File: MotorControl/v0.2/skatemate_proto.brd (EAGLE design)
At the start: 72.1 x 81.7 mm, 97 parts, among them IC1 REG1117, U1 DRV8301DCAR, U2 STM32F303XD/XELQFP64, X1 ABM3B

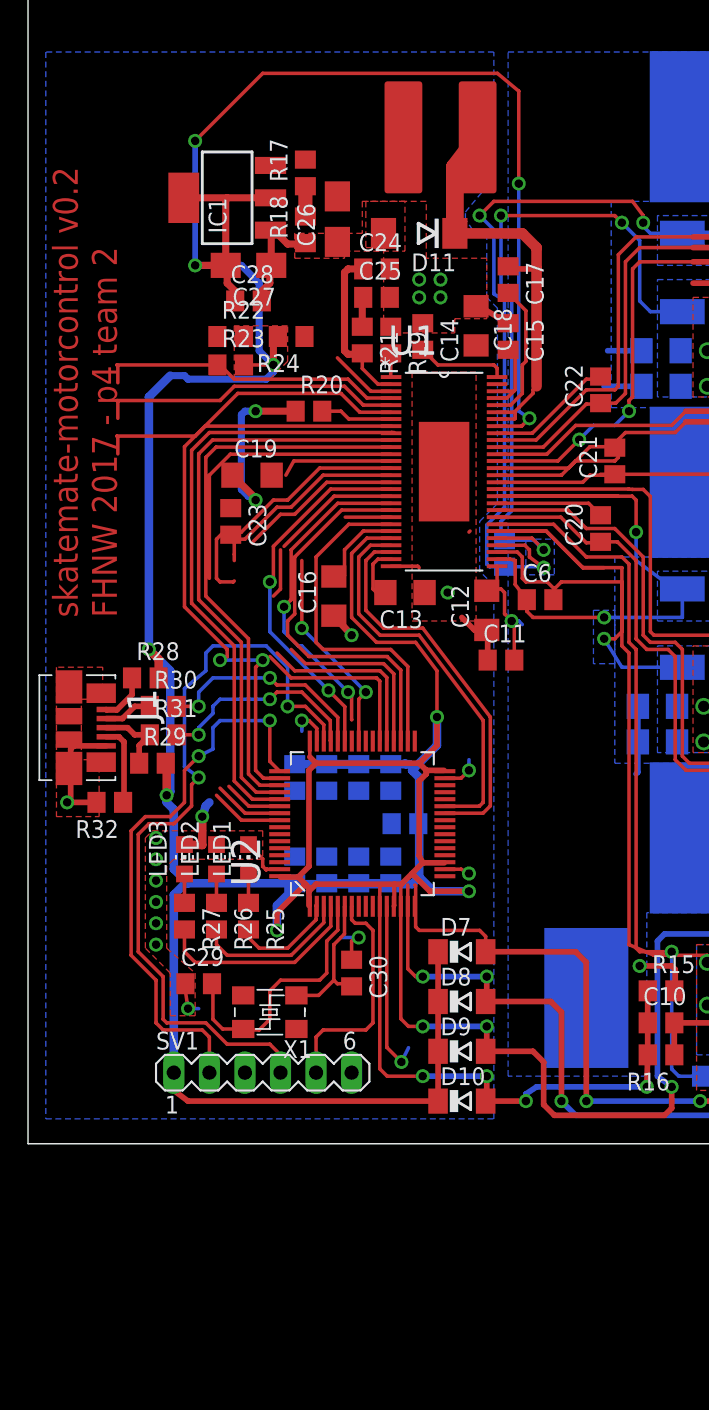
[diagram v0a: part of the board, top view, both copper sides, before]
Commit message: Add RFM module
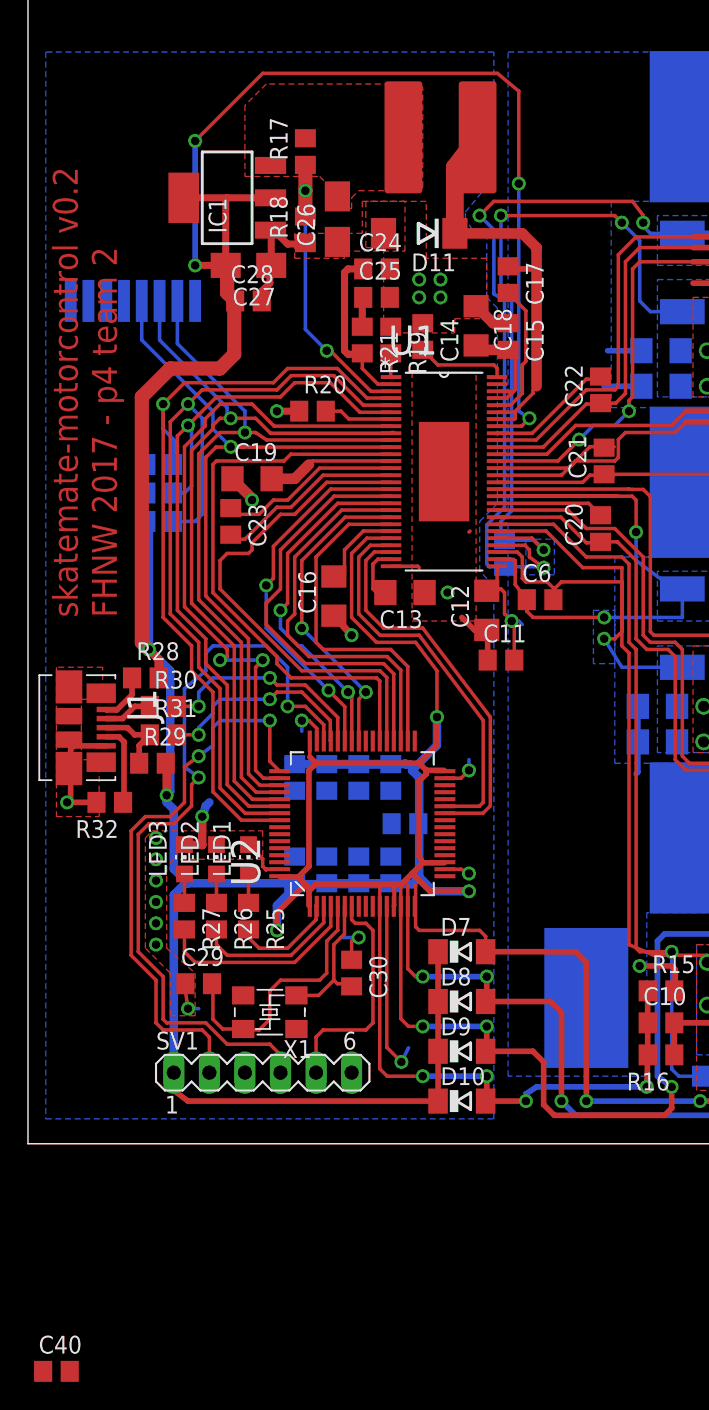
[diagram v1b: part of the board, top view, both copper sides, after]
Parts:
- added C40: 100n, skatemate:C0805
- added U3: RFM75, skatemate:RFM75
- moved R24 13.1 mm to (48.0, 47.2), flipped to the bottom, turned to 0 degrees
- moved R23 12.3 mm to (48.0, 43.2), flipped to the bottom
- moved R22 12.3 mm to (48.0, 45.2), flipped to the bottom
- moved R17 1.52 mm to (58.4, 69.6)
- moved C21 0.76 mm to (79.8, 47.5)
- moved C19 0.25 mm to (54.6, 46.2)
- moved R20 0.25 mm to (58.9, 51.1)
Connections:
- new net RFM_CE: U2.8, U3.3
- new net RFM_IRQ: U2.10, U3.8
- new net RFM_NCS: U2.9, U3.4
- net DRV_SCK: now also U3.5
- net DRV_SDI: now also U3.6
- net DRV_SDO: now also U3.7
- net GND: now also C40.2, U3.1
- net VCC: now also C40.1, U3.2
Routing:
- net DRV_NOCTW: track 26.9 -> 61.3 mm, vias 0 -> 1
- net DRV_PWRGD: track 27.1 -> 57.6 mm, vias 0 -> 1
- net DRV_NFAULT: track 26.9 -> 54.4 mm, vias 0 -> 1
- net GND: track 228.1 -> 210.2 mm
- net DRV_SCK: track 40.0 -> 55.0 mm, vias 0 -> 1
- net N$4: track 6.99 -> 21.5 mm, vias 0 -> 2
- net DRV_SDO: track 41.7 -> 53.5 mm, vias 0 -> 1
- net DRV_SDI: track 43.7 -> 55.2 mm, vias 0 -> 1
- net DRV_EN_GATE: track 24.8 -> 35.9 mm
- net DRV_DCCAL: track 33.8 -> 41.3 mm
- net N$2: track 18.8 -> 13.0 mm
- net INL_A: track 25.5 -> 30.6 mm
- net INH_C: track 18.3 -> 22.7 mm
- net SUPPLY: track 30.6 -> 33.1 mm
- net INH_B: track 23.0 -> 25.1 mm
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- added copper zone on layer 1, net +5V
- removed copper zone on layer 1, net VCC

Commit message: finished all wires and first review
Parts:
- moved C40 92.9 mm to (3.30, 67.6), flipped to the bottom
- moved R15 41.7 mm to (42.2, 11.7), turned to 90 degrees
- moved C30 40.5 mm to (21.3, 13.7), turned to 90 degrees
- moved R20 39.3 mm to (20.1, 56.9)
- moved C16 39.0 mm to (21.8, 43.7)
- moved C1 39.0 mm to (34.0, 46.5)
- moved C11 39.0 mm to (33.8, 38.9)
- moved C14 39.0 mm to (28.2, 62.0)
- moved C17 39.0 mm to (34.3, 66.0)
- moved C19 39.0 mm to (16.0, 51.8)
- moved C24 39.0 mm to (24.9, 66.8)
- moved C25 39.0 mm to (24.9, 64.8)
- moved C26 39.0 mm to (22.1, 70.4)
- moved C27 39.0 mm to (15.7, 67.1)
- moved C28 39.0 mm to (15.7, 64.5)
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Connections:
- net RFM_CE: now also U2.10; no longer U2.8
- net RFM_IRQ: now also U2.8; no longer U2.10
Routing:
- net RFM_IRQ: track 0.00 -> 94.9 mm, vias 0 -> 3
- net RFM_CE: track 0.00 -> 92.9 mm, vias 0 -> 1
- net RFM_NCS: track 0.00 -> 91.5 mm, vias 0 -> 1
- net VCC: track 320.3 -> 277.6 mm, vias 9 -> 12
- net GND: track 210.2 -> 192.2 mm, vias 42 -> 45
- net DRV_NFAULT: track 54.4 -> 61.8 mm
- net DRV_PWRGD: track 57.6 -> 64.8 mm
- net DRV_NOCTW: track 61.3 -> 68.1 mm
- net SN_B: track 45.6 -> 39.3 mm
- net GL_C: track 51.6 -> 57.3 mm
- net BST_BK: track 31.2 -> 34.7 mm
- net SSENSE: track 41.8 -> 38.5 mm
- net N$16: track 9.96 -> 13.1 mm
- net SUPPLY: track 33.1 -> 30.9 mm, vias 2 -> 5
- net BSENSE: track 139.3 -> 137.5 mm
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- added copper zone on layer 1, net N$39
- added copper zone on layer 1, net SUPPLY
- added copper zone on layer 1, net VCC
- added copper zone on layer 16, net VCC
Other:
- board size 72.1 x 81.7 mm -> 72.1 x 91.1 mm

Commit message: pretty 45
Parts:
- moved J1 1.27 mm to (4.32, 34.0)
- moved R32 1.27 mm to (4.57, 28.7)
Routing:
- net VCC: track 277.6 -> 263.6 mm
- net BST_BK: track 34.7 -> 31.7 mm
- net N$22: track 5.75 -> 8.24 mm
- net DRV_SCK: track 55.0 -> 53.0 mm
- net SUPPLY: track 30.9 -> 28.9 mm
- net PH_B: track 34.4 -> 33.1 mm
- net N$25: track 3.63 -> 4.90 mm
- net N$24: track 3.48 -> 4.75 mm
- net N$23: track 5.67 -> 6.94 mm
- net N$10: track 2.93 -> 3.48 mm
- net DRV_NCS: track 46.9 -> 46.3 mm
- net GND: track 192.2 -> 191.9 mm, vias 45 -> 46
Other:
- board text added: "Ω"

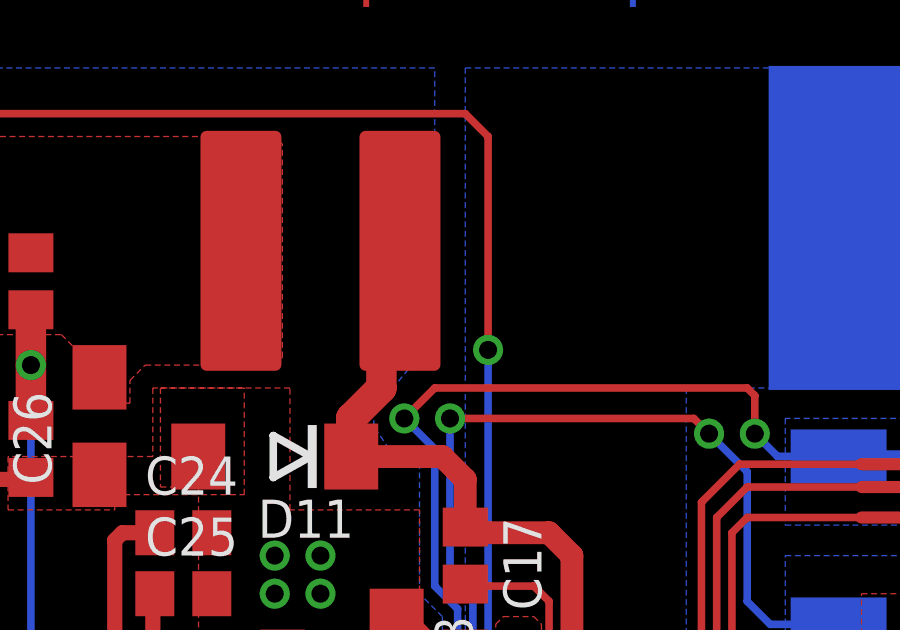
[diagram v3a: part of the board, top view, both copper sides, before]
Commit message: Layout angepasst
C ergänzt
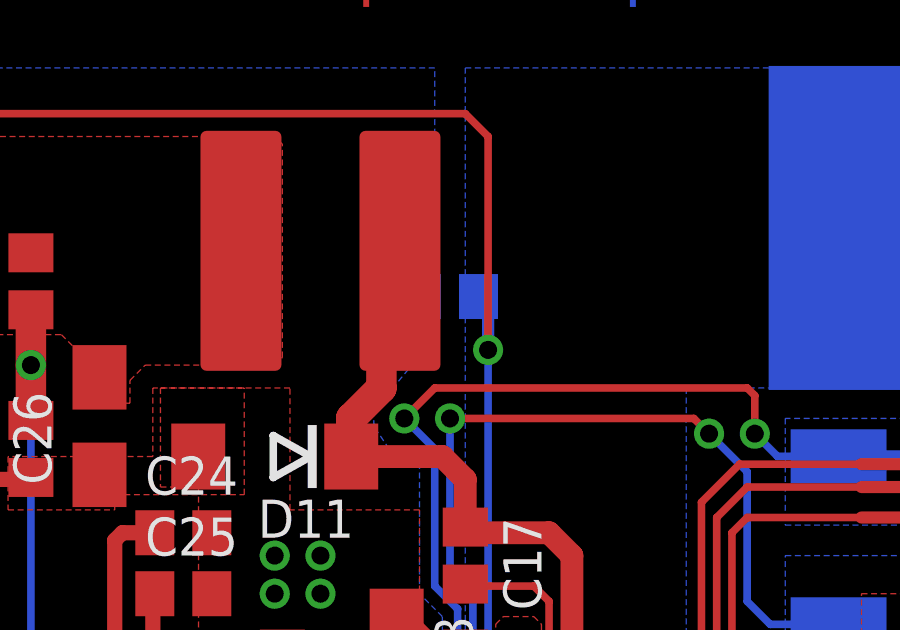
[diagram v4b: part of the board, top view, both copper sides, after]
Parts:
- added C41: 100n, skatemate:C0805
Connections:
- net GND: now also C41.2
- net VCC: now also C41.1
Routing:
- net VCC: track 263.6 -> 265.7 mm
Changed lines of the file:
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@@
 <element name="U3" library="skatemate" package="RFM75" value="RFM75" x="3.048" y="64.516" rot="MR270"/>
 <element name="C40" library="skatemate" package="C0805" value="100n" x="3.302" y="67.564" rot="MR0"/>
+<element name="C41" library="skatemate" package="C0805" value="100n" x="33.782" y="74.676" rot="MR0"/>
 </elements>
 <signals>
@@
 <wire x1="30.936" y1="30.428" x2="31.242" y2="30.734" width="0.254" layer="1"/>
 <wire x1="31.242" y1="30.734" x2="31.242" y2="31.242" width="0.254" layer="1"/>
+<contactref element="C41" pad="2"/>
 </signal>
 <signal name="N$7">
@@
 <wire x1="28.702" y1="34.29" x2="28.702" y2="33.274" width="0.254" layer="1"/>
 <wire x1="28.702" y1="33.274" x2="28.956" y2="33.02" width="0.254" layer="1"/>
+<contactref element="C41" pad="1"/>
+<wire x1="34.732" y1="74.676" x2="35.052" y2="74.676" width="0.4064" layer="16"/>
+<wire x1="35.052" y1="74.676" x2="35.052" y2="72.898" width="0.4064" layer="16"/>
 </signal>
 <signal name="INH_A">

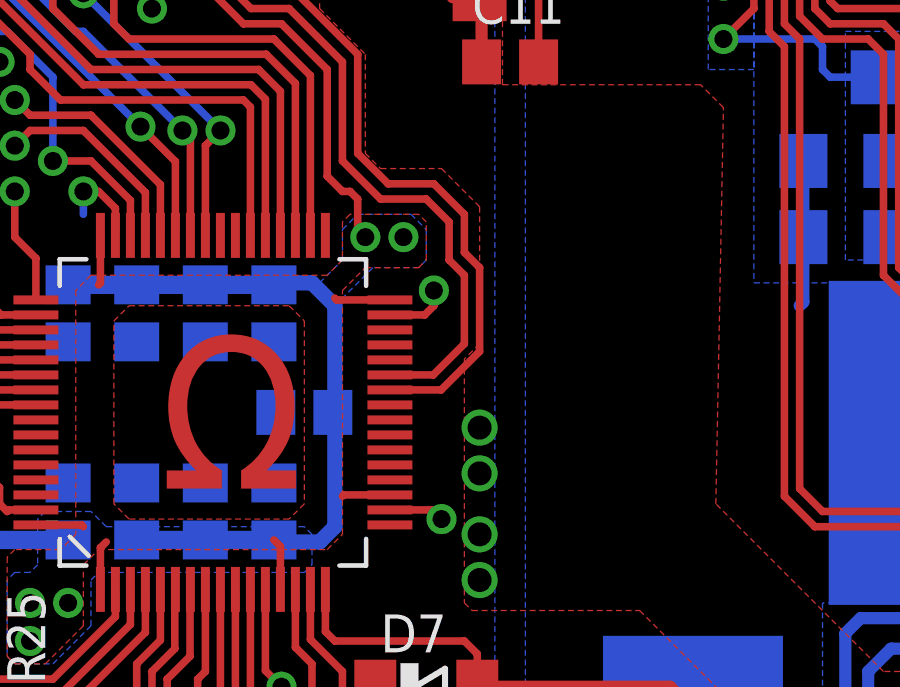
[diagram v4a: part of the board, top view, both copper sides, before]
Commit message: USART3 populated
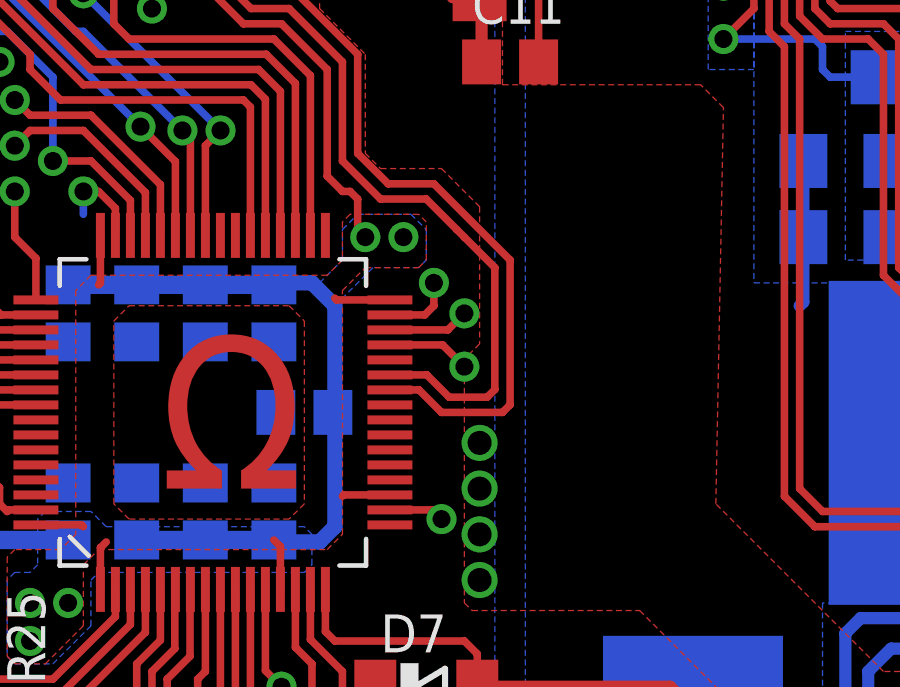
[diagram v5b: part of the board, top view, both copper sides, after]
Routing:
- net DRV_SOB: track 27.6 -> 30.7 mm
- net DRV_SOA: track 27.5 -> 30.5 mm
- net USART3_TX: track 0.00 -> 2.78 mm, vias 0 -> 1
- net USART3_RX: track 0.00 -> 2.71 mm, vias 0 -> 1
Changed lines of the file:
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@@
 <via x="26.162" y="18.034" extent="1-16" drill="0.6"/>
 <wire x1="29.776" y1="30.428" x2="30.936" y2="30.428" width="0.254" layer="1"/>
-<via x="31.242" y="31.242" extent="1-16" drill="0.6"/>
+<via x="31.242" y="31.496" extent="1-16" drill="0.6"/>
 <wire x1="29.776" y1="23.928" x2="31.19" y2="23.928" width="0.254" layer="1"/>
 <via x="31.496" y="23.622" extent="1-16" drill="0.6"/>
@@
 </polygon>
 <via x="32.766" y="21.59" extent="1-16" drill="0.8"/>
-<via x="32.766" y="26.67" extent="1-16" drill="0.8"/>
-<via x="32.766" y="25.146" extent="1-16" drill="0.8"/>
+<via x="32.766" y="26.162" extent="1-16" drill="0.8"/>
+<via x="32.766" y="24.638" extent="1-16" drill="0.8"/>
 <via x="32.766" y="23.114" extent="1-16" drill="0.8"/>
 <wire x1="41.91" y1="40.64" x2="41.91" y2="42.672" width="0.254" layer="1"/>
@@
 <wire x1="16.764" y1="64.516" x2="16.764" y2="62.23" width="0.762" layer="1"/>
 <wire x1="30.936" y1="30.428" x2="31.242" y2="30.734" width="0.254" layer="1"/>
-<wire x1="31.242" y1="30.734" x2="31.242" y2="31.242" width="0.254" layer="1"/>
+<wire x1="31.242" y1="30.734" x2="31.242" y2="31.496" width="0.254" layer="1"/>
 <contactref element="C41" pad="2"/>
 </signal>
@@
 <wire x1="25.146" y1="40.64" x2="23.622" y2="42.164" width="0.254" layer="1"/>
 <wire x1="23.622" y1="42.164" x2="23.622" y2="46.228" width="0.254" layer="1"/>
-<wire x1="29.776" y1="28.428" x2="31.222" y2="28.428" width="0.254" layer="1"/>
-<wire x1="31.75" y1="33.528" x2="31.75" y2="32.258" width="0.254" layer="1"/>
-<wire x1="31.75" y1="32.258" x2="32.258" y2="31.75" width="0.254" layer="1"/>
-<wire x1="32.258" y1="31.75" x2="32.258" y2="29.464" width="0.254" layer="1"/>
 <wire x1="25.146" y1="40.64" x2="26.416" y2="40.64" width="0.254" layer="1"/>
 <wire x1="26.416" y1="40.64" x2="28.194" y2="38.862" width="0.254" layer="1"/>
@@
 <wire x1="28.194" y1="35.56" x2="29.464" y2="34.29" width="0.254" layer="1"/>
 <wire x1="29.464" y1="34.29" x2="30.988" y2="34.29" width="0.254" layer="1"/>
-<wire x1="30.988" y1="34.29" x2="31.75" y2="33.528" width="0.254" layer="1"/>
-<wire x1="31.222" y1="28.428" x2="32.258" y2="29.464" width="0.254" layer="1"/>
+<wire x1="30.988" y1="34.29" x2="32.004" y2="33.274" width="0.254" layer="1"/>
+<wire x1="32.004" y1="33.274" x2="32.258" y2="33.02" width="0.254" layer="1"/>
+<wire x1="29.776" y1="28.428" x2="31.008" y2="28.428" width="0.254" layer="1"/>
+<wire x1="31.008" y1="28.428" x2="31.75" y2="27.686" width="0.254" layer="1"/>
+<wire x1="31.75" y1="27.686" x2="33.02" y2="27.686" width="0.254" layer="1"/>
+<wire x1="33.02" y1="27.686" x2="33.274" y2="27.94" width="0.254" layer="1"/>
+<wire x1="33.274" y1="27.94" x2="33.274" y2="32.004" width="0.254" layer="1"/>
+<wire x1="33.274" y1="32.004" x2="32.258" y2="33.02" width="0.254" layer="1"/>
 </signal>
 <signal name="DRV_SOB">
@@
 <wire x1="28.702" y1="35.814" x2="29.718" y2="34.798" width="0.254" layer="1"/>
 <wire x1="29.718" y1="34.798" x2="31.242" y2="34.798" width="0.254" layer="1"/>
-<wire x1="31.242" y1="34.798" x2="32.258" y2="33.782" width="0.254" layer="1"/>
-<wire x1="32.258" y1="33.782" x2="32.258" y2="32.512" width="0.254" layer="1"/>
-<wire x1="32.258" y1="32.512" x2="32.766" y2="32.004" width="0.254" layer="1"/>
-<wire x1="32.766" y1="32.004" x2="32.766" y2="29.21" width="0.254" layer="1"/>
-<wire x1="29.776" y1="27.928" x2="31.484" y2="27.928" width="0.254" layer="1"/>
-<wire x1="31.484" y1="27.928" x2="32.766" y2="29.21" width="0.254" layer="1"/>
+<wire x1="33.782" y1="32.258" x2="31.242" y2="34.798" width="0.254" layer="1"/>
+<wire x1="29.776" y1="27.928" x2="30.746" y2="27.928" width="0.254" layer="1"/>
+<wire x1="30.746" y1="27.928" x2="31.496" y2="27.178" width="0.254" layer="1"/>
+<wire x1="31.496" y1="27.178" x2="33.528" y2="27.178" width="0.254" layer="1"/>
+<wire x1="33.528" y1="27.178" x2="33.782" y2="27.432" width="0.254" layer="1"/>
+<wire x1="33.782" y1="27.432" x2="33.782" y2="32.258" width="0.254" layer="1"/>
 </signal>
 <signal name="SSENSE">
@@
 <signal name="USART3_RX">
 <contactref element="U2" pad="30"/>
+<via x="32.258" y="30.48" extent="1-16" drill="0.6"/>
+<wire x1="29.776" y1="29.928" x2="31.706" y2="29.928" width="0.254" layer="1"/>
+<wire x1="31.706" y1="29.928" x2="32.258" y2="30.48" width="0.254" layer="1"/>
 </signal>
 <signal name="USART3_TX">
 <contactref element="U2" pad="29"/>
+<via x="32.258" y="28.702" extent="1-16" drill="0.6"/>
+<wire x1="29.776" y1="29.428" x2="31.532" y2="29.428" width="0.254" layer="1"/>
+<wire x1="31.532" y1="29.428" x2="32.258" y2="28.702" width="0.254" layer="1"/>
 </signal>
 <signal name="N$34">
